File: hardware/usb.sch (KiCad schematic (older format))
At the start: 17 parts, among them J901 USB_OTG, U901 NX5P3090, U902 SMP1255PUTG, U903 USB3320, U904 OSC

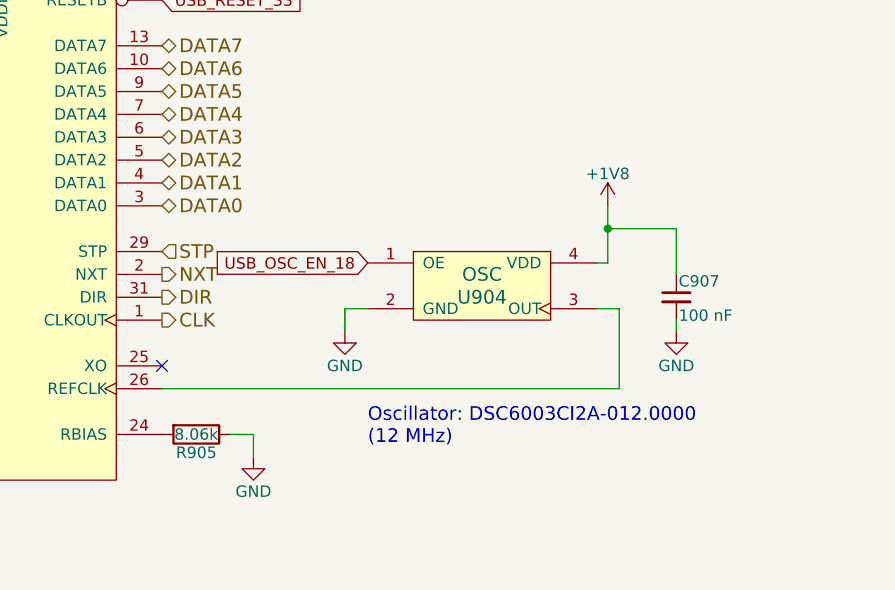
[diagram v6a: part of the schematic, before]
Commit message: Routed a first Version of the High Speed Part of the Camera Connector. The optional LVDS Clocks are left unconnected. I couldn't keep the Connectors Pin Assignment because it was just impossible to route.
WIP: general Routing

Fixed: DDR3 Trace Length Matching
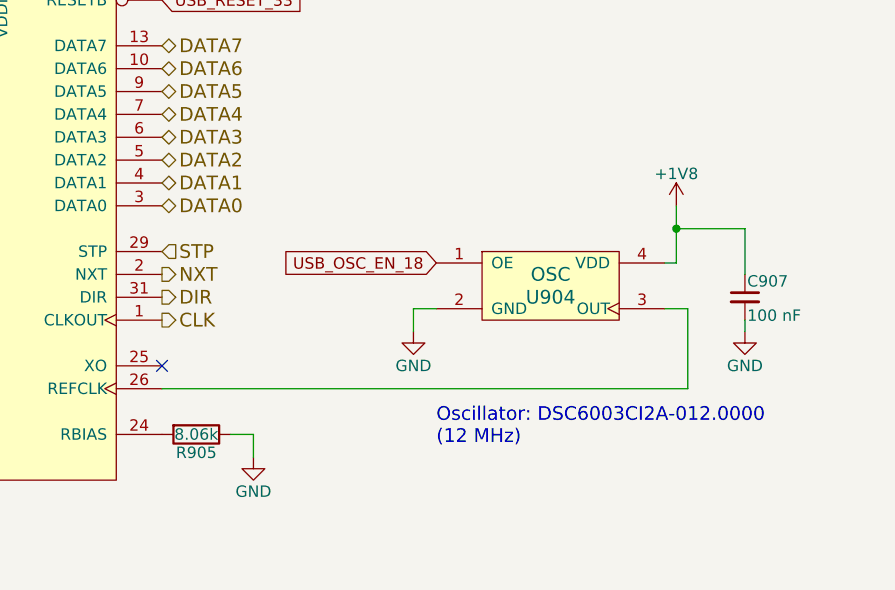
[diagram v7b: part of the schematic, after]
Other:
- moved on the sheet: C907, U904
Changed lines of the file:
@@
 $Descr A4 11693 8268
 encoding utf-8
-Sheet 8 21
+Sheet 7 21
 Title ""
 Date ""
@@
 NoConn ~ 8100 4400
 Wire Wire Line
-	8100 4500 10100 4500
-Wire Wire Line
-	10100 4500 10100 4150
-Wire Wire Line
-	10100 4150 10000 4150
+	8100 4500 10400 4500
+Wire Wire Line
+	10400 4500 10400 4150
+Wire Wire Line
+	10400 4150 10300 4150
 $Comp
 L power:GND #PWR0113
 U 1 1 5A98862B
-P 8900 4250
-F 0 "#PWR0113" H 8900 4000 50  0001 C CNN
-F 1 "GND" H 8900 4100 50  0000 C CNN
-F 2 "" H 8900 4250 50  0000 C CNN
-F 3 "" H 8900 4250 50  0000 C CNN
-	1    8900 4250
-	1    0    0    -1
-$EndComp
-Wire Wire Line
-	8900 4250 8900 4150
-Wire Wire Line
-	8900 4150 9000 4150
-Wire Wire Line
-	10050 3950 10000 3950
-Wire Wire Line
-	10050 3700 10050 3800
-Connection ~ 10050 3800
+P 9200 4250
+F 0 "#PWR0113" H 9200 4000 50  0001 C CNN
+F 1 "GND" H 9200 4100 50  0000 C CNN
+F 2 "" H 9200 4250 50  0000 C CNN
+F 3 "" H 9200 4250 50  0000 C CNN
+	1    9200 4250
+	1    0    0    -1
+$EndComp
+Wire Wire Line
+	9200 4250 9200 4150
+Wire Wire Line
+	9200 4150 9300 4150
+Wire Wire Line
+	10350 3950 10300 3950
+Wire Wire Line
+	10350 3700 10350 3800
+Connection ~ 10350 3800
 $Comp
 L power:+1V8 #PWR0114
 U 1 1 5A9888CB
-P 10050 3700
-F 0 "#PWR0114" H 10050 3550 50  0001 C CNN
-F 1 "+1V8" H 10050 3840 50  0000 C CNN
-F 2 "" H 10050 3700 50  0000 C CNN
-F 3 "" H 10050 3700 50  0000 C CNN
-	1    10050 3700
+P 10350 3700
+F 0 "#PWR0114" H 10350 3550 50  0001 C CNN
+F 1 "+1V8" H 10350 3840 50  0000 C CNN
+F 2 "" H 10350 3700 50  0000 C CNN
+F 3 "" H 10350 3700 50  0000 C CNN
+	1    10350 3700
 	1    0    0    -1
 $EndComp
@@
 L power:GND #PWR0115
 U 1 1 5A988966
-P 10350 4250
-F 0 "#PWR0115" H 10350 4000 50  0001 C CNN
-F 1 "GND" H 10350 4100 50  0000 C CNN
-F 2 "" H 10350 4250 50  0000 C CNN
-F 3 "" H 10350 4250 50  0000 C CNN
-	1    10350 4250
+P 10650 4250
+F 0 "#PWR0115" H 10650 4000 50  0001 C CNN
+F 1 "GND" H 10650 4100 50  0000 C CNN
+F 2 "" H 10650 4250 50  0000 C CNN
+F 3 "" H 10650 4250 50  0000 C CNN
+	1    10650 4250
 	1    0    0    -1
 $EndComp
@@
 Text Notes 5150 2400 0    60   ~ 0
 REFSEL[2:0] = 010\nto select 12 MHz\nREFCLK input
-Text Notes 9000 4750 0    60   ~ 0
+Text Notes 9300 4750 0    60   ~ 0
 Oscillator: DSC6003CI2A-012.0000\n(12 MHz)
 $Comp
@@
 	5150 3300 5250 3300
 Wire Wire Line
-	10050 3800 10350 3800
-Wire Wire Line
-	10050 3800 10050 3950
+	10350 3800 10650 3800
+Wire Wire Line
+	10350 3800 10350 3950
 Wire Wire Line
 	6000 3200 6000 3000
@@
 L Device:C_Small C907
 U 1 1 5B224D9D
-P 10350 4100
-F 0 "C907" H 10360 4170 50  0000 L CNN
-F 1 "100 nF" H 10360 4020 50  0000 L CNN
-F 2 "Capacitor_SMD:C_0201_0603Metric" H 10350 4100 50  0001 C CNN
-F 3 "http://search.murata.co.jp/Ceramy/image/img/A01X/G101/ENG/GRM033R60J104KE19-01.pdf" H 10350 4100 50  0001 C CNN
-F 4 "Murata Electronics North America" H 10350 4100 50  0001 C CNN "MFG Name"
-F 5 "GRM033R60J104KE19D" H 10350 4100 50  0001 C CNN "MFG Part Num"
-F 6 "490-3167-1-ND" H 10350 4100 50  0001 C CNN "Digikey"
-F 7 "1" H 10350 4100 50  0001 C CNN "Populated"
-F 8 "CAP CER 0.1UF 6.3V X5R 0201" H 10350 4100 50  0001 C CNN "Description"
-F 9 "SPEC" H 10350 4100 50  0001 C CNN "Source"
-F 10 "1" H 10350 4100 50  0001 C CNN "Populate for SBGA485(Z-7030)"
-F 11 "1" H 10350 4100 50  0001 C CNN "Populate for CLG484(Z-7012s/Z-7015)"
-	1    10350 4100
+P 10650 4100
+F 0 "C907" H 10660 4170 50  0000 L CNN
+F 1 "100 nF" H 10660 4020 50  0000 L CNN
+F 2 "Capacitor_SMD:C_0201_0603Metric" H 10650 4100 50  0001 C CNN
+F 3 "http://search.murata.co.jp/Ceramy/image/img/A01X/G101/ENG/GRM033R60J104KE19-01.pdf" H 10650 4100 50  0001 C CNN
+F 4 "Murata Electronics North America" H 10650 4100 50  0001 C CNN "MFG Name"
+F 5 "GRM033R60J104KE19D" H 10650 4100 50  0001 C CNN "MFG Part Num"
+F 6 "490-3167-1-ND" H 10650 4100 50  0001 C CNN "Digikey"
+F 7 "1" H 10650 4100 50  0001 C CNN "Populated"
+F 8 "CAP CER 0.1UF 6.3V X5R 0201" H 10650 4100 50  0001 C CNN "Description"
+F 9 "SPEC" H 10650 4100 50  0001 C CNN "Source"
+F 10 "1" H 10650 4100 50  0001 C CNN "Populate for SBGA485(Z-7030)"
+F 11 "1" H 10650 4100 50  0001 C CNN "Populate for CLG484(Z-7012s/Z-7015)"
+	1    10650 4100
 	1    0    0    -1
 $EndComp
@@
 	7350 1950 7350 2000
 Wire Wire Line
-	10350 4200 10350 4250
-Wire Wire Line
-	10350 3800 10350 4000
+	10650 4200 10650 4250
+Wire Wire Line
+	10650 3800 10650 4000
 $Comp
 L Device:C_Small C903
@@
 L osc:OSC U904
 U 1 1 5A98852C
-P 9500 4050
-F 0 "U904" H 9500 4000 60  0000 C CNN
-F 1 "OSC" H 9500 4100 60  0000 C CNN
-F 2 "footprints:Microchip_CDFN_3.2x2.5mm" H 9500 4050 60  0001 C CNN
-F 3 "http://www.microchip.com/mymicrochip/filehandler.aspx?ddocname=en587489" H 9500 4050 60  0001 C CNN
-F 4 "Microchip Technology" H 9500 4050 60  0001 C CNN "MFG Name"
-F 5 "DSC6003CI2A-012.0000" H 9500 4050 60  0001 C CNN "MFG Part Num"
-F 6 "DSC6003CI2A-012.0000-ND" H 9500 4050 60  0001 C CNN "Digikey"
-F 7 "579-C6003CI2A0120000" H 9500 4050 60  0001 C CNN "Mouser"
-F 8 "1" H 9500 4050 60  0001 C CNN "Populated"
-F 9 "SPEC" H 9500 4050 60  0001 C CNN "Source"
-F 10 "1" H 9500 4050 50  0001 C CNN "Populate for SBGA485(Z-7030)"
-F 11 "1" H 9500 4050 50  0001 C CNN "Populate for CLG484(Z-7012s/Z-7015)"
-	1    9500 4050
-	1    0    0    -1
-$EndComp
-Text GLabel 9000 3950 0    50   Input ~ 0
+P 9800 4050
+F 0 "U904" H 9800 4000 60  0000 C CNN
+F 1 "OSC" H 9800 4100 60  0000 C CNN
+F 2 "footprints:Microchip_CDFN_3.2x2.5mm" H 9800 4050 60  0001 C CNN
+F 3 "http://www.microchip.com/mymicrochip/filehandler.aspx?ddocname=en587489" H 9800 4050 60  0001 C CNN
+F 4 "Microchip Technology" H 9800 4050 60  0001 C CNN "MFG Name"
+F 5 "DSC6003CI2A-012.0000" H 9800 4050 60  0001 C CNN "MFG Part Num"
+F 6 "DSC6003CI2A-012.0000-ND" H 9800 4050 60  0001 C CNN "Digikey"
+F 7 "579-C6003CI2A0120000" H 9800 4050 60  0001 C CNN "Mouser"
+F 8 "1" H 9800 4050 60  0001 C CNN "Populated"
+F 9 "SPEC" H 9800 4050 60  0001 C CNN "Source"
+F 10 "1" H 9800 4050 50  0001 C CNN "Populate for SBGA485(Z-7030)"
+F 11 "1" H 9800 4050 50  0001 C CNN "Populate for CLG484(Z-7012s/Z-7015)"
+	1    9800 4050
+	1    0    0    -1
+$EndComp
+Text GLabel 9300 3950 0    50   Input ~ 0
 USB_OSC_EN_18
 $EndSCHEMATC
